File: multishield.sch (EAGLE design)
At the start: 13 parts, among them J2 2x16p-2.54, J4 2x6p-2.54, M1 ARDUINO_R3_ICSP, SW1 SK-12D01, U1 AD595AQ-DIP14, U2 ATMEGA328P_PDIP

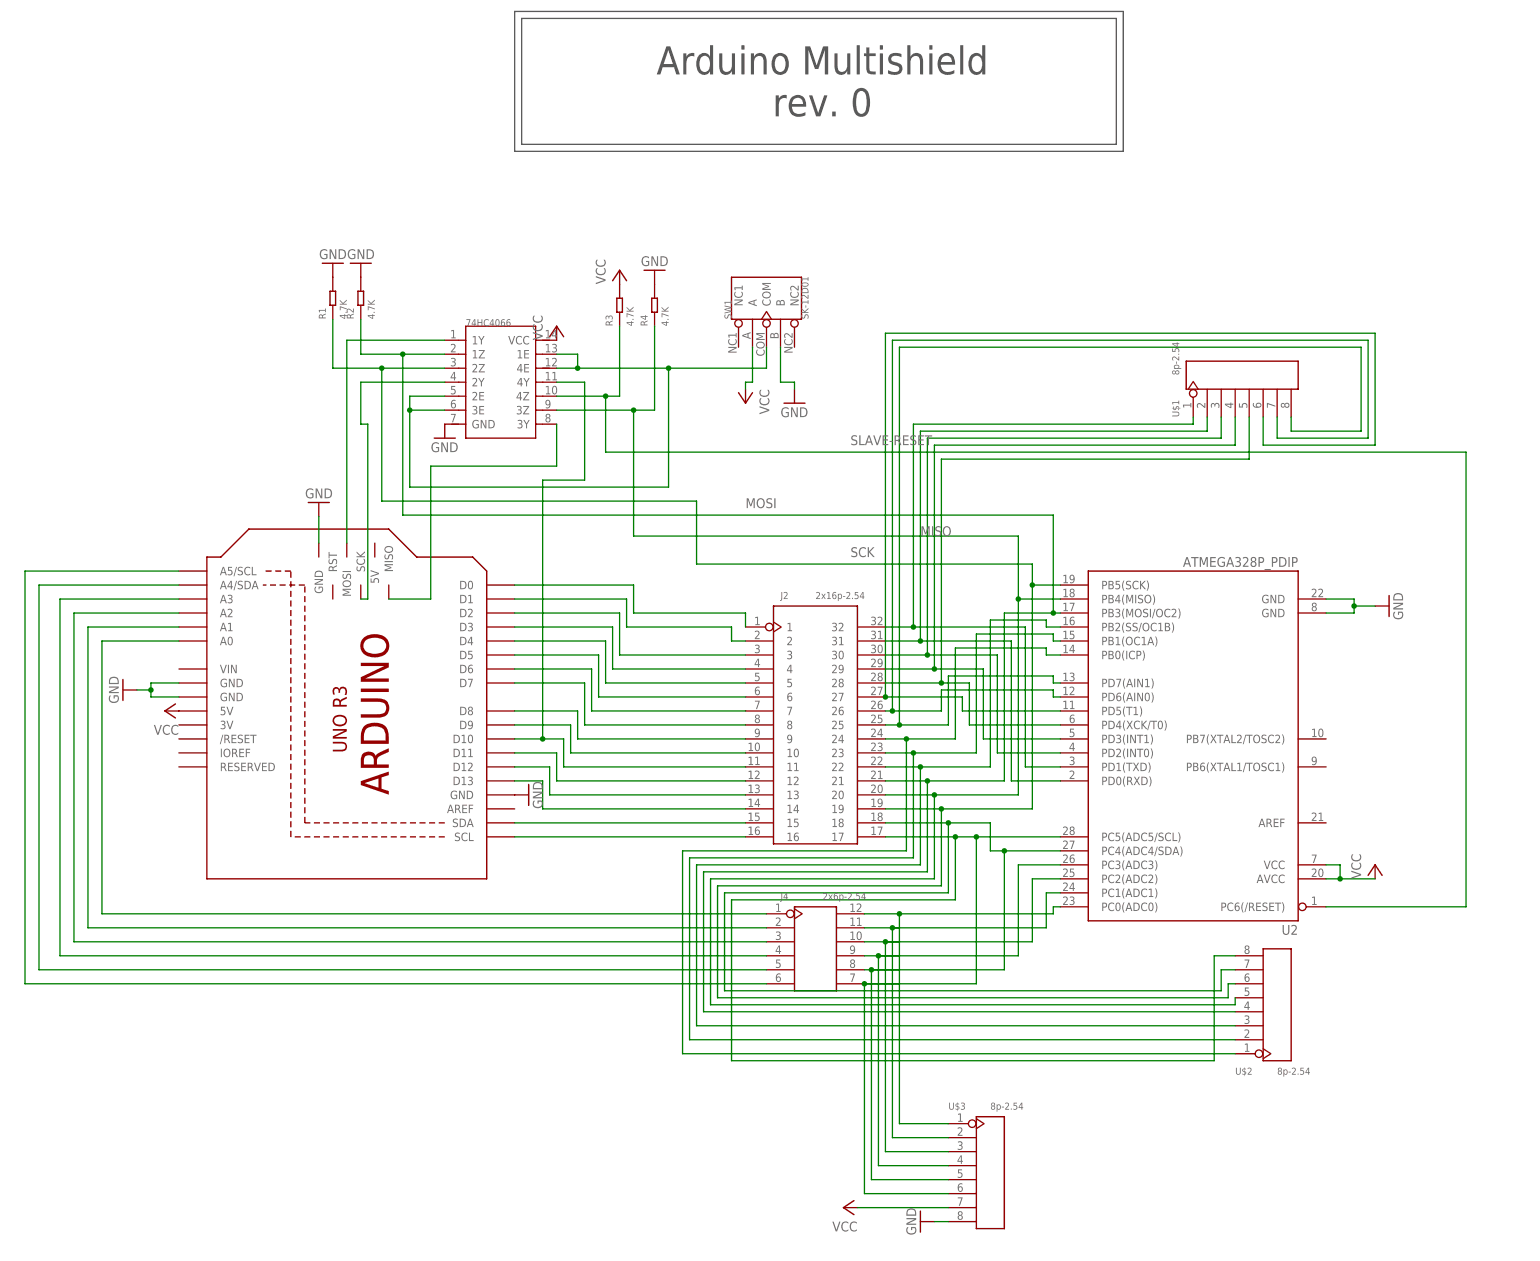
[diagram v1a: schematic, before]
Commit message: added most of the things by now, minor aesthetic additions left for rev.0
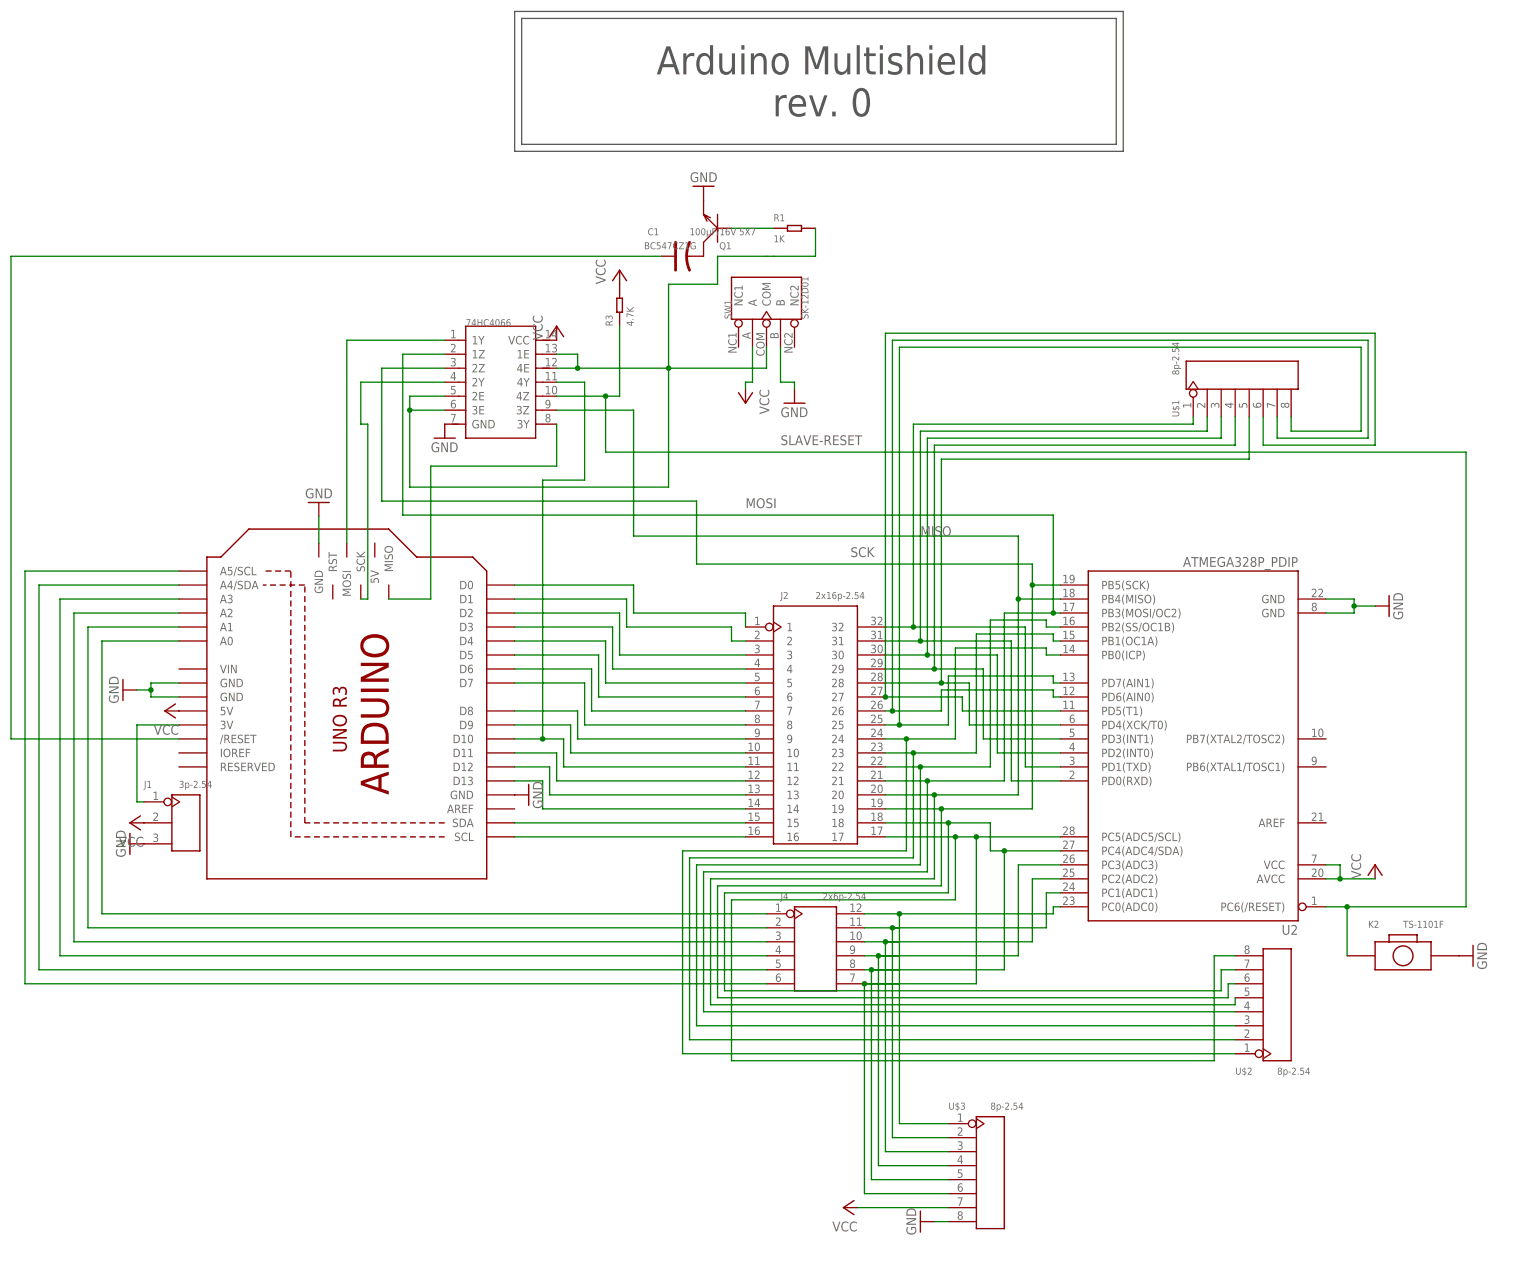
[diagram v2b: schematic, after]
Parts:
- removed R2, R4: 4.7K, Seeed-OPL-Resistor:DIP-RES-4.7K-5%-1/4W(PR-D2.3XL6.5MM)
- added C1: 100µF/16V 5X7, Seeed-OPL-Capacitor:DIP-CAP-ALUMINUM-47UF-16V(D5-H9MM)
- added J1: 3p-2.54, Seeed-OPL-Connector:DIP-BLACK-FEMALE-HEADER-VERT(3P-2.54)
- added K2: TS-1101F, Seeed-OPL-Button:DIP-BUTTON-FRONT-WHITE(2P-3.4X6MM)
- added Q1: BC547CZ1G, Seeed-OPL-Transistor:DIP-TRANSISTOR-NPN-45V-0.1A-BC547CZ1G(TO-92)
- R1: value 4.7K -> 1K; device Seeed-OPL-Resistor:DIP-RES-4.7K-5%-1/4W(PR-D2.3XL6.5MM) -> Seeed-OPL-Resistor:DIP-RES-1K-5%-1/4W(PR-D2.3XL6.5MM)
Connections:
- new net N$36: C1.-, Q1.C
- new net N$37: C1.+, M1./RESET
- new net N$38: Q1.B, R1.1
- new net N$54: J1.P$1, M1.3V
- net GND: now also J1.P$3, K2.2, Q1.E; no longer R1.2, R2.2, R4.2
- net MISO: no longer R4.1
- net MOSI: no longer R2.1
- net N$56: now also R1.2
- net SCK: no longer R1.1
- net SLAVE-RESET: now also K2.1
- net VCC: now also J1.P$2
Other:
- moved on the sheet: R1
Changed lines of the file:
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@@
 <part name="GND3" library="supply1" deviceset="GND" device=""/>
 <part name="GND4" library="supply1" deviceset="GND" device=""/>
-<part name="GND5" library="supply1" deviceset="GND" device=""/>
 <part name="GND7" library="supply1" deviceset="GND" device=""/>
 <part name="P+3" library="supply1" deviceset="VCC" device=""/>
 <part name="SW1" library="Seeed-OPL-Button" deviceset="DIP-TOGGLE-SWITCH-ON-ON(3+2P-8.8X4.6MM)" device="" value="SK-12D01"/>
 <part name="P+4" library="supply1" deviceset="VCC" device=""/>
-<part name="R1" library="Seeed-OPL-Resistor" deviceset="DIP-RES-4.7K-5%-1/4W(PR-D2.3XL6.5MM)" device="" value="4.7K"/>
-<part name="R2" library="Seeed-OPL-Resistor" deviceset="DIP-RES-4.7K-5%-1/4W(PR-D2.3XL6.5MM)" device="" value="4.7K"/>
 <part name="R3" library="Seeed-OPL-Resistor" deviceset="DIP-RES-4.7K-5%-1/4W(PR-D2.3XL6.5MM)" device="" value="4.7K"/>
-<part name="R4" library="Seeed-OPL-Resistor" deviceset="DIP-RES-4.7K-5%-1/4W(PR-D2.3XL6.5MM)" device="" value="4.7K"/>
-<part name="GND6" library="supply1" deviceset="GND" device=""/>
-<part name="GND9" library="supply1" deviceset="GND" device=""/>
 <part name="P+5" library="supply1" deviceset="VCC" device=""/>
 <part name="U$1" library="Seeed-OPL-Connector" deviceset="DIP-BLACK-MALE-HEADER-VERT(8P-2.54)" device="" value="8p-2.54"/>
@@
 <part name="GND10" library="supply1" deviceset="GND" device=""/>
 <part name="P+6" library="supply1" deviceset="VCC" device=""/>
+<part name="GND11" library="supply1" deviceset="GND" device=""/>
+<part name="K2" library="Seeed-OPL-Button" deviceset="DIP-BUTTON-FRONT-WHITE(2P-3.4X6MM)" device="" value="TS-1101F"/>
+<part name="C1" library="Seeed-OPL-Capacitor" deviceset="DIP-CAP-ALUMINUM-47UF-16V(D5-H9MM)" device="" value="100µF/16V  5X7"/>
+<part name="Q1" library="Seeed-OPL-Transistor" deviceset="DIP-TRANSISTOR-NPN-45V-0.1A-BC547CZ1G(TO-92)" device="" value="BC547CZ1G"/>
+<part name="GND5" library="supply1" deviceset="GND" device=""/>
+<part name="R1" library="Seeed-OPL-Resistor" deviceset="DIP-RES-1K-5%-1/4W(PR-D2.3XL6.5MM)" device="" value="1K"/>
+<part name="J1" library="Seeed-OPL-Connector" deviceset="DIP-BLACK-FEMALE-HEADER-VERT(3P-2.54)" device="" value="3p-2.54"/>
+<part name="GND6" library="supply1" deviceset="GND" device=""/>
+<part name="P+7" library="supply1" deviceset="VCC" device=""/>
 </parts>
 <sheets>
@@
 <instance part="GND3" gate="1" x="160.02" y="74.93" rot="R90"/>
 <instance part="GND4" gate="1" x="121.92" y="128.016" rot="R180"/>
-<instance part="GND5" gate="1" x="129.54" y="171.45" rot="R180"/>
 <instance part="GND7" gate="1" x="144.78" y="139.7"/>
 <instance part="P+3" gate="VCC" x="165.1" y="160.02"/>
 <instance part="SW1" gate="G$1" x="203.2" y="165.1" rot="R90"/>
 <instance part="P+4" gate="VCC" x="199.39" y="146.05" rot="R180"/>
-<instance part="R1" gate="G$1" x="124.46" y="165.1" rot="R90"/>
-<instance part="R2" gate="G$1" x="129.54" y="165.1" rot="R90"/>
 <instance part="R3" gate="G$1" x="176.53" y="163.83" rot="R90"/>
-<instance part="R4" gate="G$1" x="182.88" y="163.83" rot="R90"/>
-<instance part="GND6" gate="1" x="124.46" y="171.45" rot="R180"/>
-<instance part="GND9" gate="1" x="182.88" y="170.18" rot="R180"/>
 <instance part="P+5" gate="VCC" x="176.53" y="170.18"/>
 <instance part="U$1" gate="G$1" x="289.56" y="151.13" rot="R90"/>
@@
 <instance part="GND10" gate="1" x="231.14" y="-2.54" rot="R270"/>
 <instance part="P+6" gate="VCC" x="217.17" y="0" rot="R90"/>
+<instance part="GND11" gate="1" x="331.47" y="45.72" rot="R90"/>
+<instance part="K2" gate="G$1" x="318.77" y="45.72"/>
+<instance part="C1" gate="G$1" x="187.96" y="172.72"/>
+<instance part="Q1" gate="G$1" x="194.31" y="177.8" rot="R180"/>
+<instance part="GND5" gate="1" x="191.77" y="185.42" rot="R180"/>
+<instance part="R1" gate="G$1" x="208.28" y="177.8"/>
+<instance part="J1" gate="G$1" x="97.79" y="69.85"/>
+<instance part="GND6" gate="1" x="87.63" y="66.04" rot="R270"/>
+<instance part="P+7" gate="VCC" x="87.63" y="69.85" rot="R90"/>
 </instances>
 <busses>
@@
 <wire x1="256.54" y1="107.95" x2="255.27" y2="107.95" width="0.1524" layer="91"/>
 <wire x1="255.27" y1="107.95" x2="255.27" y2="125.73" width="0.1524" layer="91"/>
-<pinref part="R2" gate="G$1" pin="1"/>
-<wire x1="129.54" y1="161.29" x2="129.54" y2="154.94" width="0.1524" layer="91"/>
 <pinref part="U1" gate="74HC4066" pin="1Z"/>
-<wire x1="129.54" y1="154.94" x2="137.16" y2="154.94" width="0.1524" layer="91"/>
-<junction x="137.16" y="154.94"/>
 <wire x1="137.16" y1="154.94" x2="144.78" y2="154.94" width="0.1524" layer="91"/>
 <wire x1="255.27" y1="125.73" x2="137.16" y2="125.73" width="0.1524" layer="91"/>
@@
 <wire x1="219.71" y1="0" x2="236.22" y2="0" width="0.1524" layer="91"/>
 </segment>
+<segment>
+<pinref part="J1" gate="G$1" pin="P$2"/>
+<pinref part="P+7" gate="VCC" pin="VCC"/>
+</segment>
 </net>
 <net name="GND" class="0">
@@
 </segment>
 <segment>
-<pinref part="R1" gate="G$1" pin="2"/>
-<pinref part="GND6" gate="1" pin="GND"/>
-</segment>
-<segment>
-<pinref part="R4" gate="G$1" pin="2"/>
-<pinref part="GND9" gate="1" pin="GND"/>
-</segment>
-<segment>
-<pinref part="R2" gate="G$1" pin="2"/>
-<pinref part="GND5" gate="1" pin="GND"/>
-</segment>
-<segment>
 <pinref part="SW1" gate="G$1" pin="B"/>
 <wire x1="205.74" y1="156.21" x2="205.74" y2="149.86" width="0.1524" layer="91"/>
@@
 <pinref part="U$3" gate="G$1" pin="8"/>
 <wire x1="233.68" y1="-2.54" x2="236.22" y2="-2.54" width="0.1524" layer="91"/>
+</segment>
+<segment>
+<pinref part="K2" gate="G$1" pin="2"/>
+<pinref part="GND11" gate="1" pin="GND"/>
+</segment>
+<segment>
+<pinref part="Q1" gate="G$1" pin="E"/>
+<pinref part="GND5" gate="1" pin="GND"/>
+</segment>
+<segment>
+<pinref part="J1" gate="G$1" pin="P$3"/>
+<pinref part="GND6" gate="1" pin="GND"/>
 </segment>
 </net>
@@
 <pinref part="SW1" gate="G$1" pin="COM"/>
 <wire x1="203.2" y1="152.4" x2="203.2" y2="156.21" width="0.1524" layer="91"/>
+<wire x1="185.42" y1="152.4" x2="185.42" y2="167.64" width="0.1524" layer="91"/>
+<wire x1="185.42" y1="167.64" x2="194.31" y2="167.64" width="0.1524" layer="91"/>
+<wire x1="194.31" y1="167.64" x2="194.31" y2="172.72" width="0.1524" layer="91"/>
+<wire x1="194.31" y1="172.72" x2="203.2" y2="172.72" width="0.1524" layer="91"/>
+<pinref part="R1" gate="G$1" pin="2"/>
+<wire x1="203.2" y1="172.72" x2="204.47" y2="172.72" width="0.1524" layer="91"/>
+<wire x1="204.47" y1="172.72" x2="212.09" y2="172.72" width="0.1524" layer="91"/>
+<wire x1="212.09" y1="172.72" x2="212.09" y2="177.8" width="0.1524" layer="91"/>
 </segment>
 </net>
 <net name="SCK" class="0">
 <segment>
-<pinref part="R1" gate="G$1" pin="1"/>
-<wire x1="124.46" y1="161.29" x2="124.46" y2="152.4" width="0.1524" layer="91"/>
 <pinref part="U1" gate="74HC4066" pin="2Z"/>
-<wire x1="124.46" y1="152.4" x2="133.35" y2="152.4" width="0.1524" layer="91"/>
-<junction x="133.35" y="152.4"/>
 <wire x1="133.35" y1="152.4" x2="144.78" y2="152.4" width="0.1524" layer="91"/>
 <wire x1="133.35" y1="152.4" x2="133.35" y2="128.27" width="0.1524" layer="91"/>
@@
 <junction x="173.99" y="147.32"/>
 <pinref part="U2" gate="G$1" pin="PC6(/RESET)"/>
-<wire x1="304.8" y1="54.61" x2="330.2" y2="54.61" width="0.1524" layer="91"/>
+<wire x1="304.8" y1="54.61" x2="308.61" y2="54.61" width="0.1524" layer="91"/>
+<wire x1="308.61" y1="54.61" x2="330.2" y2="54.61" width="0.1524" layer="91"/>
 <wire x1="330.2" y1="54.61" x2="330.2" y2="137.16" width="0.1524" layer="91"/>
 <wire x1="330.2" y1="137.16" x2="173.99" y2="137.16" width="0.1524" layer="91"/>
 <wire x1="173.99" y1="137.16" x2="173.99" y2="147.32" width="0.1524" layer="91"/>
-<label x="218.44" y="138.43" size="1.778" layer="95"/>
+<label x="205.74" y="138.43" size="1.778" layer="95"/>
+<junction x="308.61" y="54.61"/>
+<pinref part="K2" gate="G$1" pin="1"/>
+<wire x1="308.61" y1="45.72" x2="308.61" y2="54.61" width="0.1524" layer="91"/>
 </segment>
 </net>
@@
 <segment>
 <pinref part="U1" gate="74HC4066" pin="3Z"/>
-<pinref part="R4" gate="G$1" pin="1"/>
 <wire x1="165.1" y1="144.78" x2="179.07" y2="144.78" width="0.1524" layer="91"/>
-<wire x1="179.07" y1="144.78" x2="182.88" y2="144.78" width="0.1524" layer="91"/>
-<wire x1="182.88" y1="144.78" x2="182.88" y2="160.02" width="0.1524" layer="91"/>
-<junction x="179.07" y="144.78"/>
 <wire x1="179.07" y1="144.78" x2="179.07" y2="121.92" width="0.1524" layer="91"/>
 <pinref part="J2" gate="G$1" pin="20"/>
@@
 </segment>
 </net>
+<net name="N$36" class="0">
+<segment>
+<pinref part="C1" gate="G$1" pin="-"/>
+<pinref part="Q1" gate="G$1" pin="C"/>
+</segment>
+</net>
+<net name="N$37" class="0">
+<segment>
+<pinref part="M1" gate="G$1" pin="/RESET"/>
+<wire x1="96.52" y1="85.09" x2="66.04" y2="85.09" width="0.1524" layer="91"/>
+<wire x1="66.04" y1="85.09" x2="66.04" y2="172.72" width="0.1524" layer="91"/>
+<pinref part="C1" gate="G$1" pin="+"/>
+<wire x1="66.04" y1="172.72" x2="184.15" y2="172.72" width="0.1524" layer="91"/>
+</segment>
+</net>
+<net name="N$38" class="0">
+<segment>
+<pinref part="Q1" gate="G$1" pin="B"/>
+<wire x1="204.47" y1="177.8" x2="196.85" y2="177.8" width="0.1524" layer="91"/>
+<pinref part="R1" gate="G$1" pin="1"/>
+</segment>
+</net>
+<net name="N$54" class="0">
+<segment>
+<pinref part="J1" gate="G$1" pin="P$1"/>
+<wire x1="90.17" y1="73.66" x2="88.9" y2="73.66" width="0.1524" layer="91"/>
+<wire x1="88.9" y1="73.66" x2="88.9" y2="87.63" width="0.1524" layer="91"/>
+<pinref part="M1" gate="G$1" pin="3V"/>
+<wire x1="88.9" y1="87.63" x2="96.52" y2="87.63" width="0.1524" layer="91"/>
+</segment>
+</net>
